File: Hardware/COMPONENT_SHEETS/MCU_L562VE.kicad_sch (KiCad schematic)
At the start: 29 parts, among them SW1 MCU Reset, U9 STM32L562VET6Q, Y2 32MHz

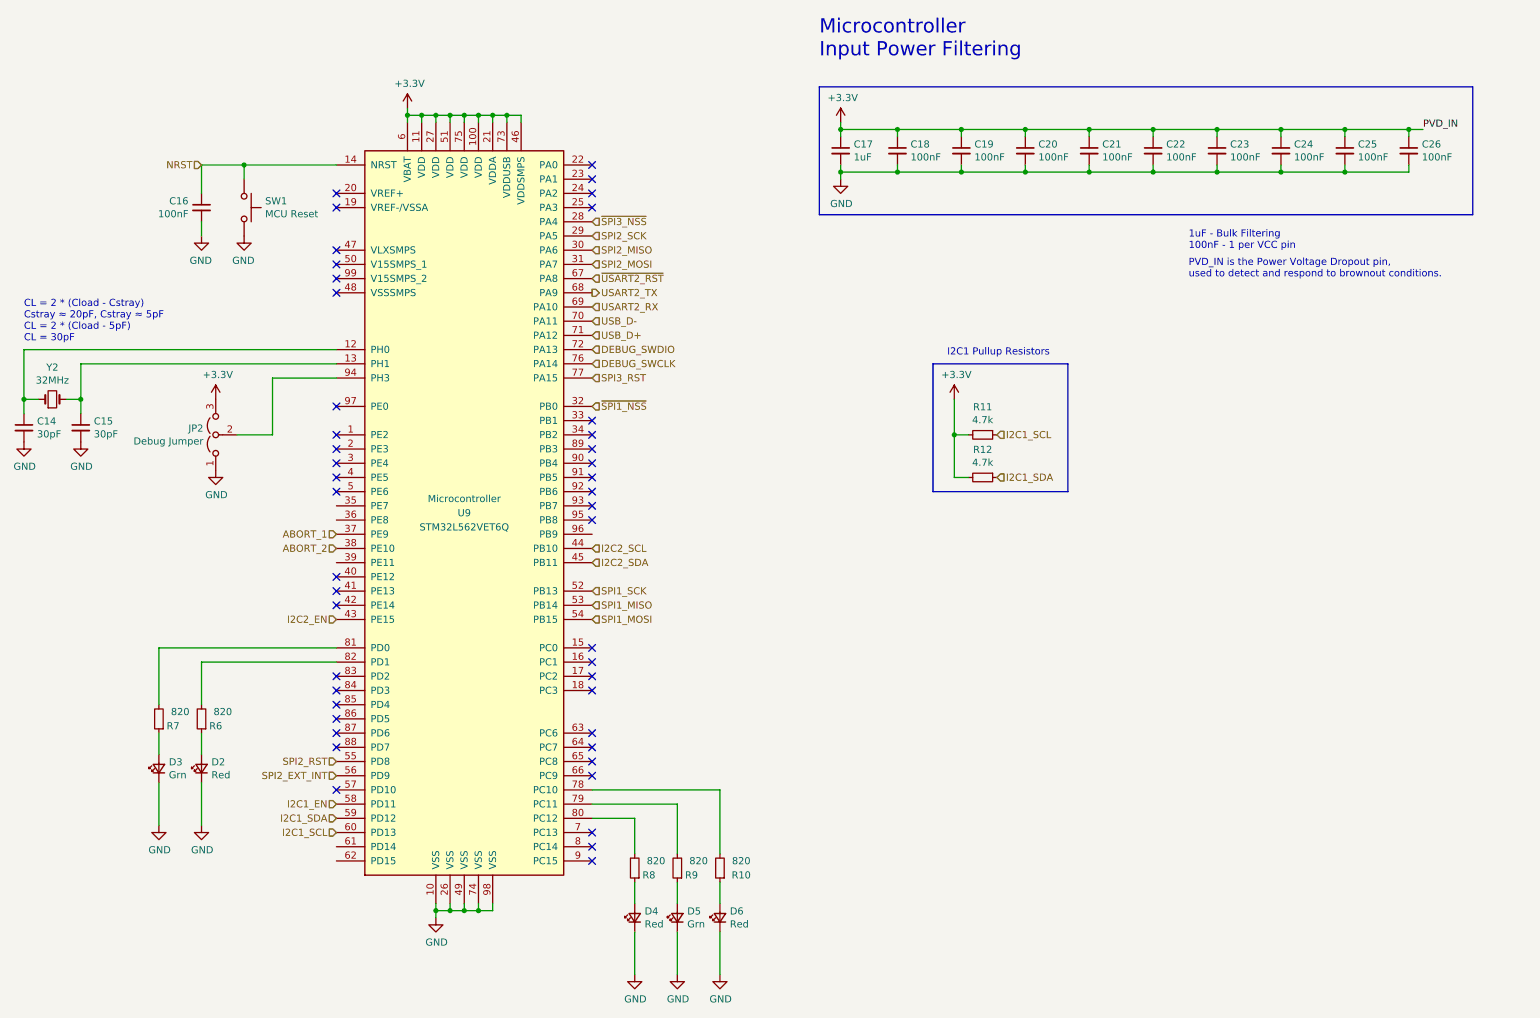
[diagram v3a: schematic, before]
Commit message: Adjusted component spacing, corrected MCU schematic, added cutout for USB, moved SMA inwards
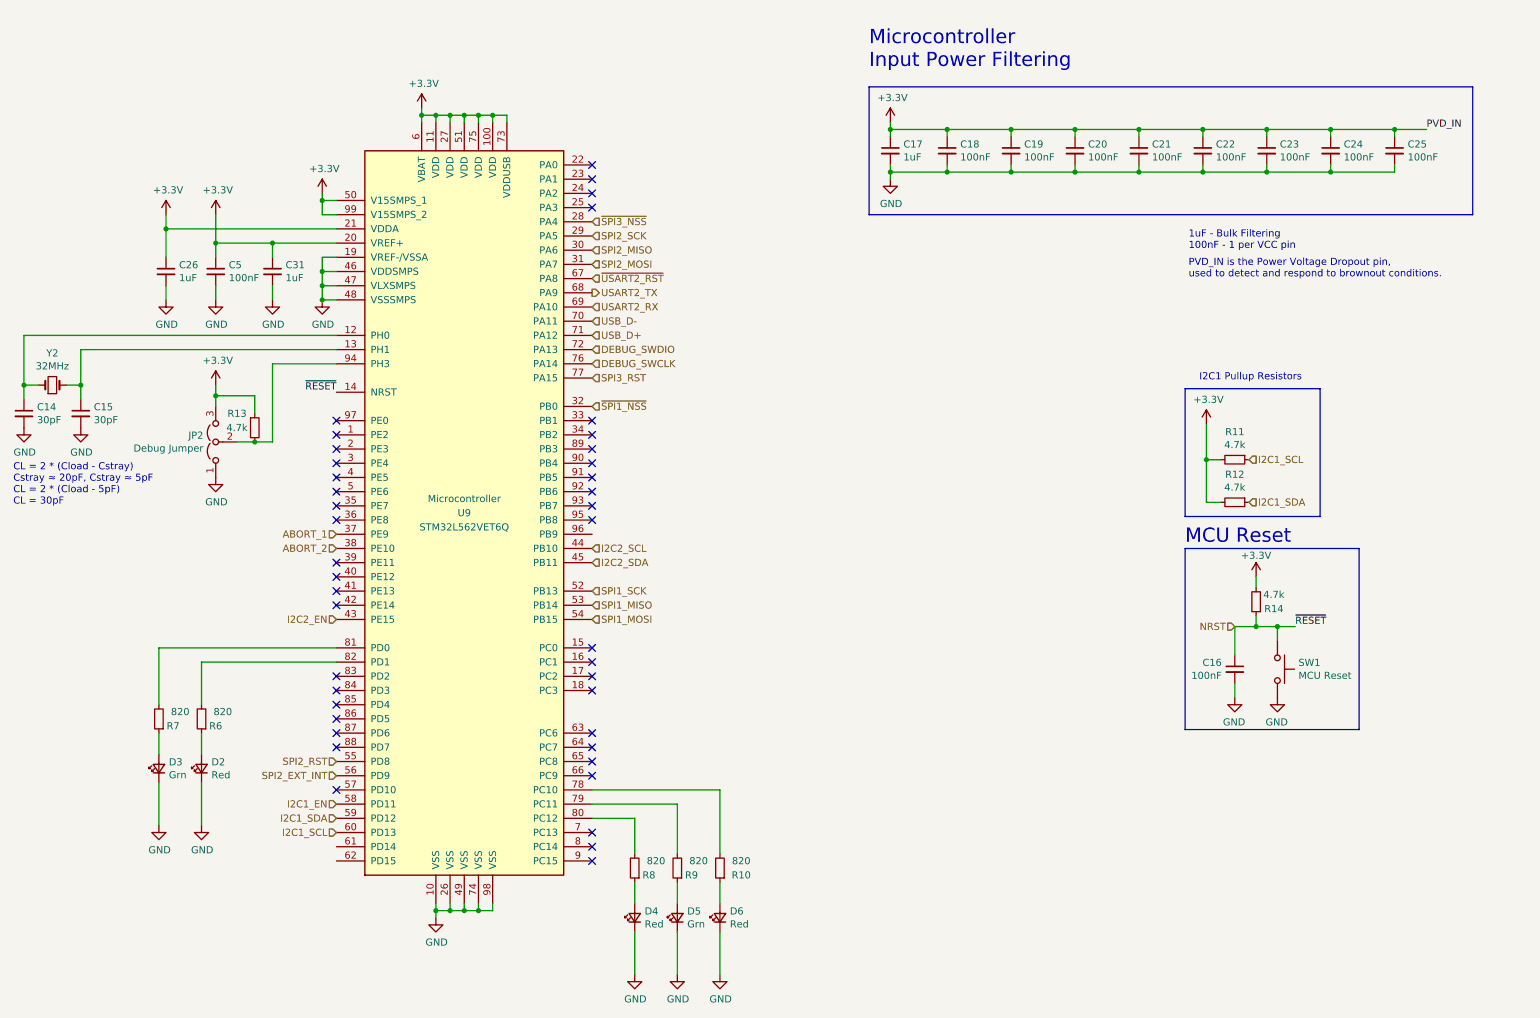
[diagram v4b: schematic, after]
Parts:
- added C31: 1uF, Capacitor_SMD:C_0603_1608Metric_Pad1.08x0.95mm_HandSolder, symbol Device:C_Small
- added C5: 100nF, Capacitor_SMD:C_0603_1608Metric_Pad1.08x0.95mm_HandSolder, symbol Device:C_Small
- added R13: 4.7k, Resistor_SMD:R_0603_1608Metric_Pad0.98x0.95mm_HandSolder, symbol Device:R_Small
- added R14: 4.7k, Resistor_SMD:R_0603_1608Metric_Pad1.05x0.95mm_HandSolder, symbol Device:R_Small
- C26: value 100nF -> 1uF
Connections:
- net +3V3: now also U9.20 (VREF+), U9.50 (V15SMPS_1), U9.99 (V15SMPS_2), C31.1, C5.1, R13.1, R14.2; no longer U9.46 (VDDSMPS)
- net GND: now also U9.19 (VREF-/VSSA), U9.46 (VDDSMPS), U9.47 (VLXSMPS), U9.48 (VSSSMPS), C31.2, C5.2
- net NRST: now also R14.1
- net at JP2.2 (C), U9.94 (PH3): now also R13.2
- no-connect marks 45 -> 42
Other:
- note added: "MCU Reset"
- moved on the sheet: C14, C15, C17, C18, C19, C20, C21, C22, C23, C24, C25, JP2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
